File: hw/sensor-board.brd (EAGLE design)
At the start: 50 x 40 mm, 49 parts, among them U1 LT1762EMS8-3.3PBF, U2 ULN2003LVPWR, U3 ULN2003LVPWR, U4 PCA9685PW, U5 AT42QT1070-SSU, X1 MOLEX-501953-0407, X2 MOLEX-501953-0407

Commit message: Fix sourcing info for components.
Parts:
- C1: device rcl:C0603K -> rcl:C0805K
- C13: value 0.01uF 16V -> 0.01uF 25V
- C2: value 0.01uF 100V -> 0.01uF 25V
- C3: device rcl:C0402K -> rcl:C0603K
- C4: value 0.01uF 100V -> 0.1uF 100V
- moved C1 1.50 mm to (20.0, 34.2)
- moved C2 0.25 mm to (20.0, 32.2)
- moved C3 0.25 mm to (15.0, 34.2)
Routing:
- net VDD_3_3: track 28.3 -> 49.6 mm, vias 2 -> 3
- net GND: track 67.6 -> 64.5 mm
- net VDD_5: track 150.8 -> 150.3 mm

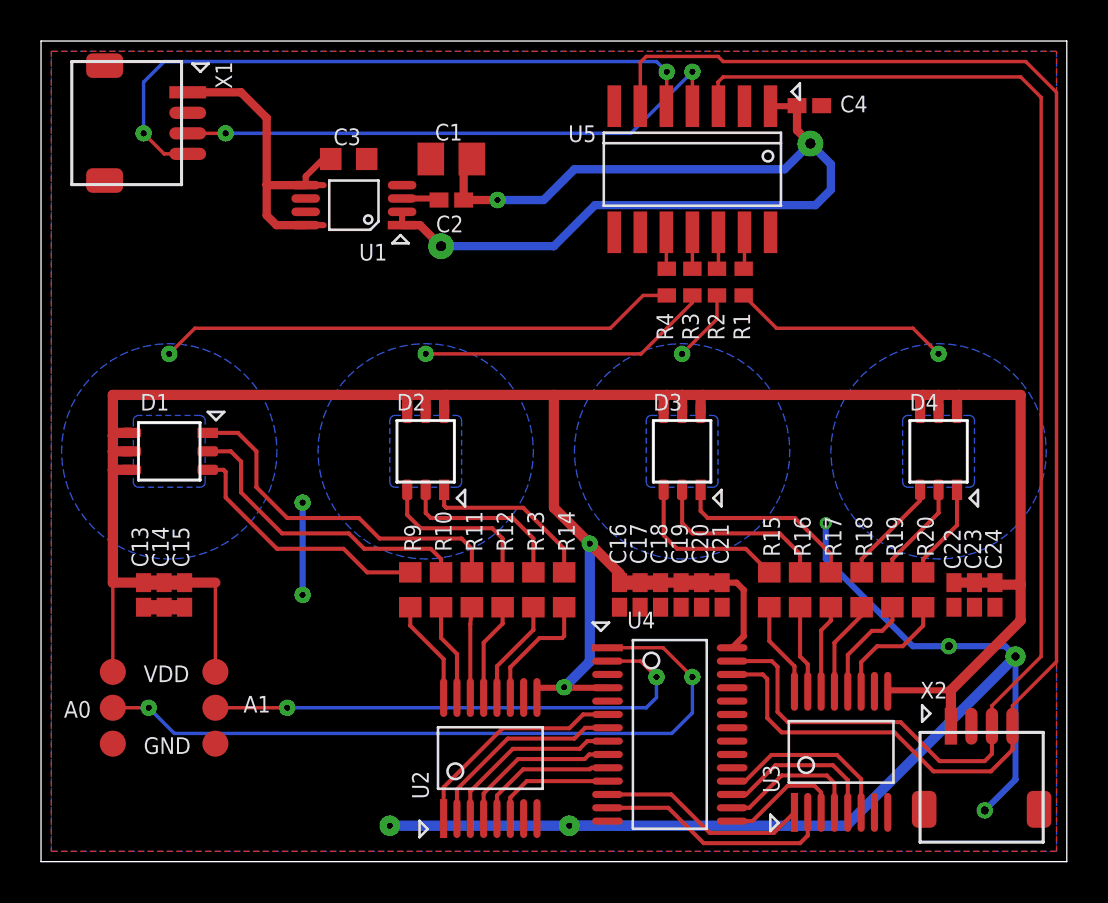
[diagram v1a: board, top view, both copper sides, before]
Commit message: Create option to share LDO between sensor boards.
This is done to reduce the BOM. If necessary, the voltage regulator can
be installed later on as the land pattern stays.

Label connector signals.

Adjust some silkscreen positions.
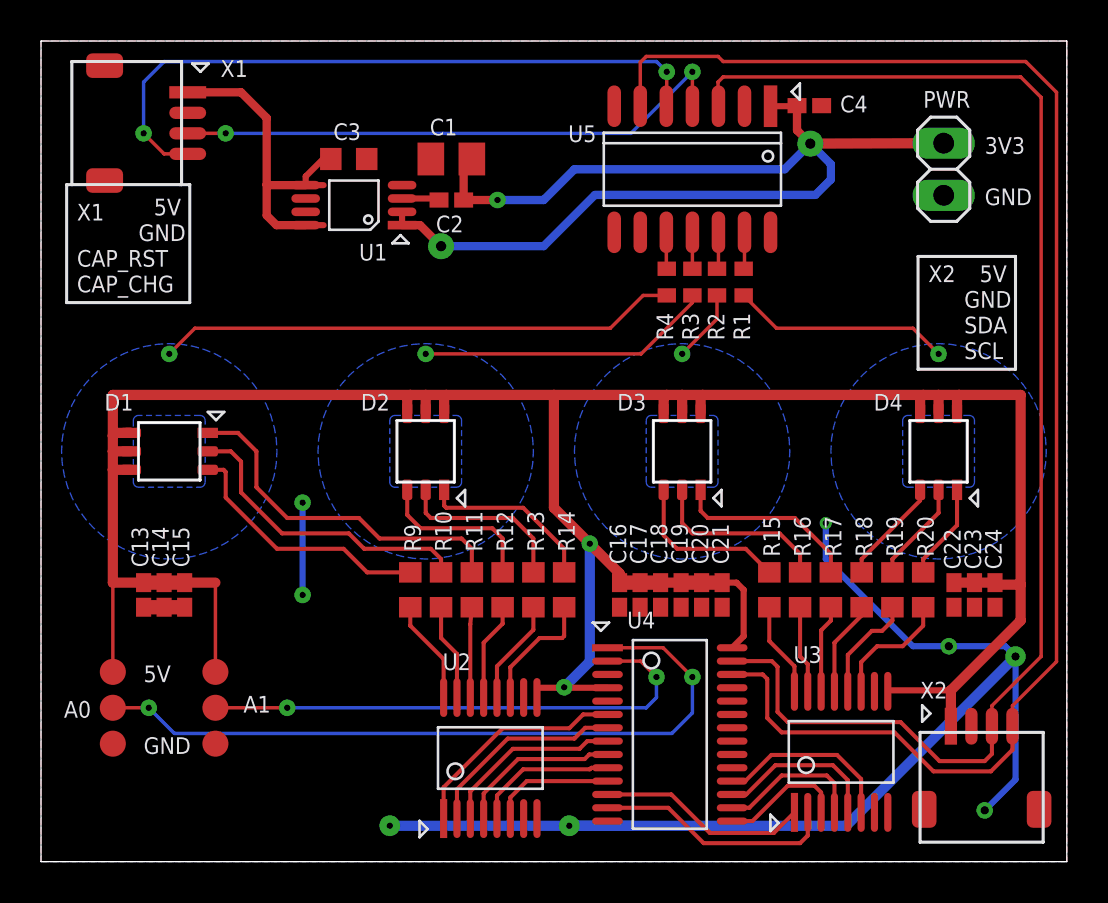
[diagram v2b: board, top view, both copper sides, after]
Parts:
- added PWR: (no value), pinhead:1X02
- renumbered VDD to 5V
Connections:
- net GND: now also PWR.2, X1.5, X1.6, X2.5, X2.6
- net VDD_3_3: now also PWR.1
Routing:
- net VDD_3_3: track 49.6 -> 55.8 mm
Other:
- board text added: "3V3"
- board text added: "5V"
- board text added: "CAP_CHG"
- board text added: "CAP_RST"
- board text added: "GND"
- board text added: "SCL"
- board text added: "SDA"
- board text added: "X1"
- board text added: "X2"

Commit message: Add pullup to capsense change line.
Capsense schematic and layout checked wrt datasheet.
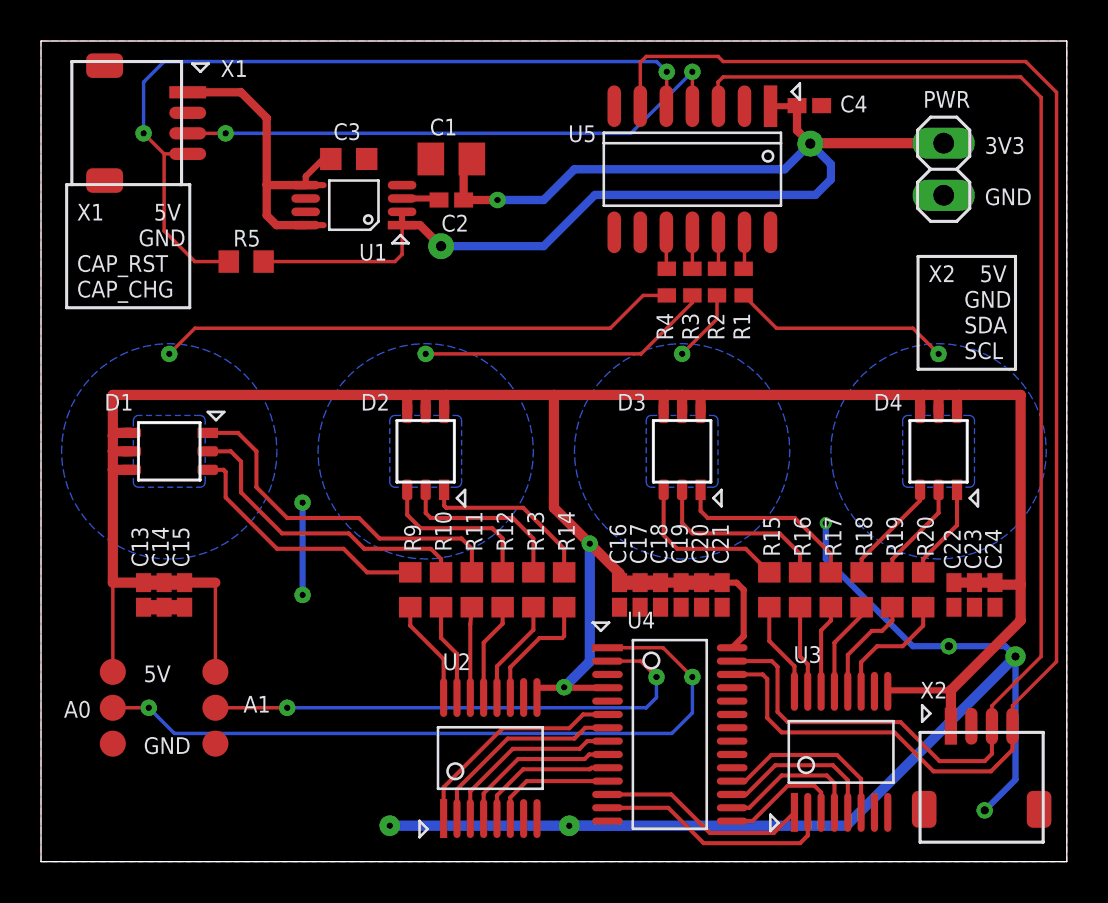
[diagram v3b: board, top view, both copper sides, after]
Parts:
- added R5: 47k, myrcl:R0603
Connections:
- net !CAPSENSE_CHG!: now also R5.1
- net VDD_3_3: now also R5.2
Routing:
- net VDD_3_3: track 55.8 -> 64.2 mm
- net !CAPSENSE_CHG!: track 32.9 -> 40.4 mm
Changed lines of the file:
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@@
 <text x="46" y="34.5" size="0.8128" layer="21" font="vector">3V3</text>
 <text x="46" y="32" size="0.8128" layer="21" font="vector">GND</text>
-<text x="5.5" y="31.5" size="0.8128" layer="21" font="vector">5V</text>
-<text x="4.75" y="30.25" size="0.8128" layer="21" font="vector">GND</text>
-<text x="1.75" y="29" size="0.8128" layer="21" font="vector">CAP_RST</text>
-<text x="1.75" y="27.75" size="0.8128" layer="21" font="vector">CAP_CHG</text>
+<text x="5.5" y="31.25" size="0.8128" layer="21" font="vector">5V</text>
+<text x="4.75" y="30" size="0.8128" layer="21" font="vector">GND</text>
+<text x="1.75" y="28.75" size="0.8128" layer="21" font="vector">CAP_RST</text>
+<text x="1.75" y="27.5" size="0.8128" layer="21" font="vector">CAP_CHG</text>
 <wire x1="1.5" y1="33" x2="1.25" y2="33" width="0.15" layer="21"/>
-<wire x1="1.25" y1="33" x2="1.25" y2="27.25" width="0.15" layer="21"/>
-<wire x1="1.25" y1="27.25" x2="7.25" y2="27.25" width="0.15" layer="21"/>
-<wire x1="7.25" y1="27.25" x2="7.25" y2="33" width="0.15" layer="21"/>
+<wire x1="1.25" y1="33" x2="1.25" y2="27" width="0.15" layer="21"/>
+<wire x1="1.25" y1="27" x2="7.25" y2="27" width="0.15" layer="21"/>
+<wire x1="7.25" y1="27" x2="7.25" y2="33" width="0.15" layer="21"/>
 <wire x1="7.25" y1="33" x2="6.75" y2="33" width="0.15" layer="21"/>
 <text x="43.25" y="28.25" size="0.8128" layer="21" font="vector">X2</text>
@@
 <attribute name="ELEMENT14_URL" value="http://sg.element14.com/jsp/search/productdetail.jsp?sku=1692285" x="20" y="32.25" size="1.778" layer="27" display="off"/>
 <attribute name="MFR_PART" value="C0402C103J3RACTU" x="20" y="32.25" size="1.778" layer="27" display="off"/>
-<attribute name="NAME" x="19.25" y="30.675" size="0.8128" layer="25" font="vector"/>
+<attribute name="NAME" x="20.85" y="31.525" size="0.8128" layer="25" font="vector" rot="R180"/>
 <attribute name="VALUE" x="19.5" y="30.8" size="1.016" layer="27"/>
 </element>
@@
 <attribute name="NAME" x="43" y="36.75" size="0.8128" layer="25" font="vector" ratio="10"/>
 <attribute name="VALUE" x="40.825" y="36.29" size="1.27" layer="27" rot="R270"/>
+</element>
+<element name="R5" library="myrcl" package="R0603" value="47k" x="10" y="29.25">
+<attribute name="ELEMENT14_URL" value="http://sg.element14.com/jsp/search/productdetail.jsp?sku=1799462" x="10" y="29.25" size="0.8128" layer="27" display="off"/>
+<attribute name="MFR_PART" value="RC0603JR-1047KL" x="10" y="29.25" size="0.8128" layer="27" display="off"/>
 </element>
 </elements>
@@
 <contactref element="C23" pad="1"/>
 <contactref element="C24" pad="1"/>
-<polygon width="0.16" layer="1" spacing="0.8128" pour="hatch" isolate="0.3048">
+<polygon width="0.2" layer="1" spacing="0.8128" pour="hatch" isolate="0.3048">
 <vertex x="0" y="40"/>
 <vertex x="0" y="0"/>
@@
 <wire x1="36.85" y1="35.65" x2="36.85" y2="36.85" width="0.4064" layer="1"/>
 <wire x1="37.75" y1="32.5" x2="27" y2="32.5" width="0.4064" layer="16"/>
-<wire x1="25" y1="30" x2="24.5" y2="30" width="0" layer="19" extent="1-16"/>
 <via x="19.5" y="30" extent="1-16" drill="0.5" diameter="1.27"/>
 <wire x1="24.5" y1="30" x2="19.5" y2="30" width="0.4064" layer="16"/>
@@
 <wire x1="20.6" y1="32.25" x2="20.6" y2="33.85" width="0.4064" layer="1"/>
 <wire x1="20.6" y1="33.85" x2="21" y2="34.25" width="0.4064" layer="1"/>
-<contactref element="PWR" pad="1"/>
-<wire x1="44" y1="35.02" x2="37.5" y2="35" width="0.5" layer="1"/>
 <wire x1="27" y1="32.5" x2="24.5" y2="30" width="0.4" layer="16"/>
 <wire x1="37.75" y1="32.5" x2="38.5" y2="33.25" width="0.4" layer="16"/>
 <wire x1="38.5" y1="33.25" x2="38.5" y2="34" width="0.4" layer="16"/>
 <wire x1="38.5" y1="34" x2="37.5" y2="35" width="0.4" layer="16"/>
+<contactref element="PWR" pad="1"/>
+<wire x1="44" y1="35.02" x2="37.5" y2="35.02" width="0.5" layer="1"/>
+<wire x1="37.5" y1="35.02" x2="37.5" y2="35" width="0.5" layer="1"/>
+<contactref element="R5" pad="2"/>
+<wire x1="17.6" y1="31.025" x2="17.6" y2="29.6" width="0.17" layer="1"/>
+<wire x1="17.6" y1="29.6" x2="17.25" y2="29.25" width="0.17" layer="1"/>
+<wire x1="17.25" y1="29.25" x2="10.85" y2="29.25" width="0.17" layer="1"/>
 </signal>
 <signal name="N$8">
@@
 <wire x1="5" y1="35.5" x2="6" y2="34.5" width="0.17" layer="1"/>
 <wire x1="6" y1="34.5" x2="7.15" y2="34.5" width="0.17" layer="1"/>
+<contactref element="R5" pad="1"/>
+<wire x1="6" y1="34.5" x2="6" y2="30.75" width="0.17" layer="1"/>
+<wire x1="6" y1="30.75" x2="7.5" y2="29.25" width="0.17" layer="1"/>
+<wire x1="7.5" y1="29.25" x2="9.15" y2="29.25" width="0.17" layer="1"/>
 </signal>
 <signal name="N$6">
